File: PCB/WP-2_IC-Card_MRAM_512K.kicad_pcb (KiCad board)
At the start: 2 copper layers, 54 x 54 mm, 38 parts, among them J1 SMS-138-01-G-S, SW1 CUS-14TB, U1 MR2A08xxYSxxx, U2 MIC5317-3.3YD5, U3 4245, U4 4245, U5 4245, U6 4245

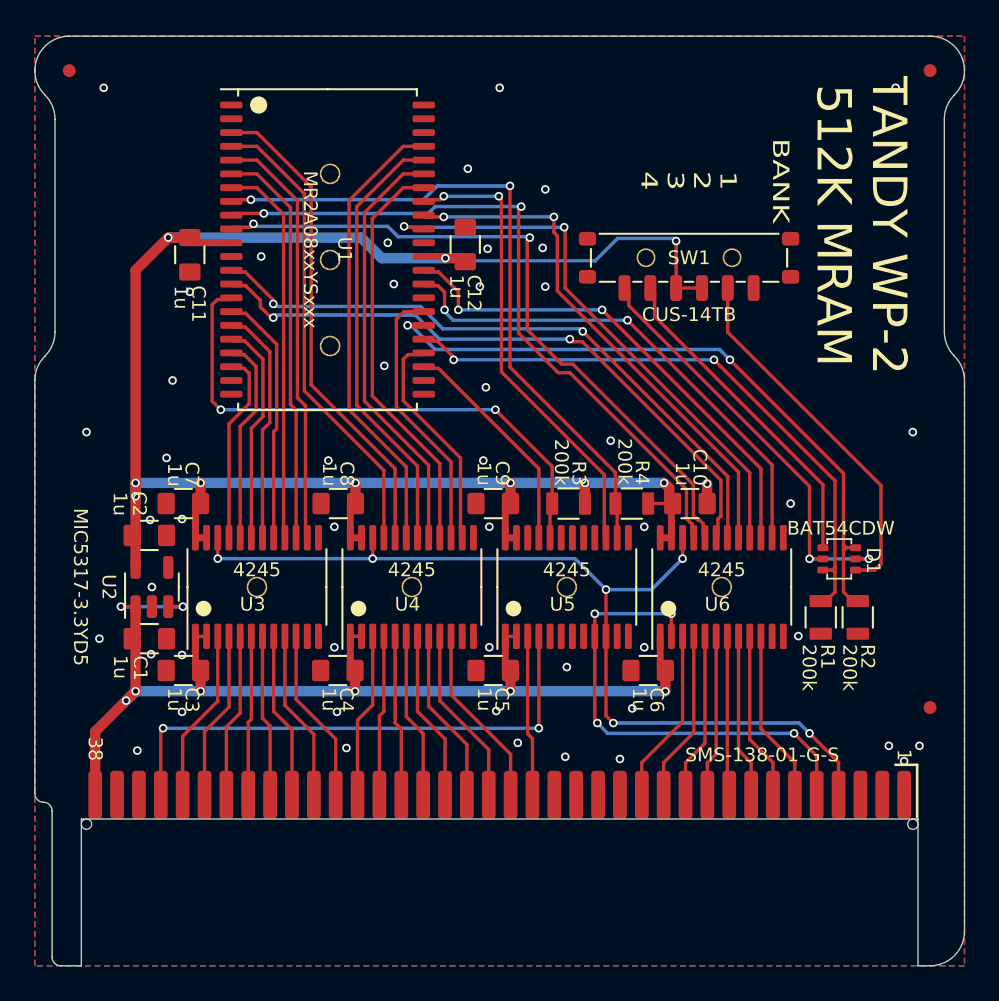
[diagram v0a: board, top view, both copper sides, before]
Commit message: local symbol & footprint library organization, add shielded mram version
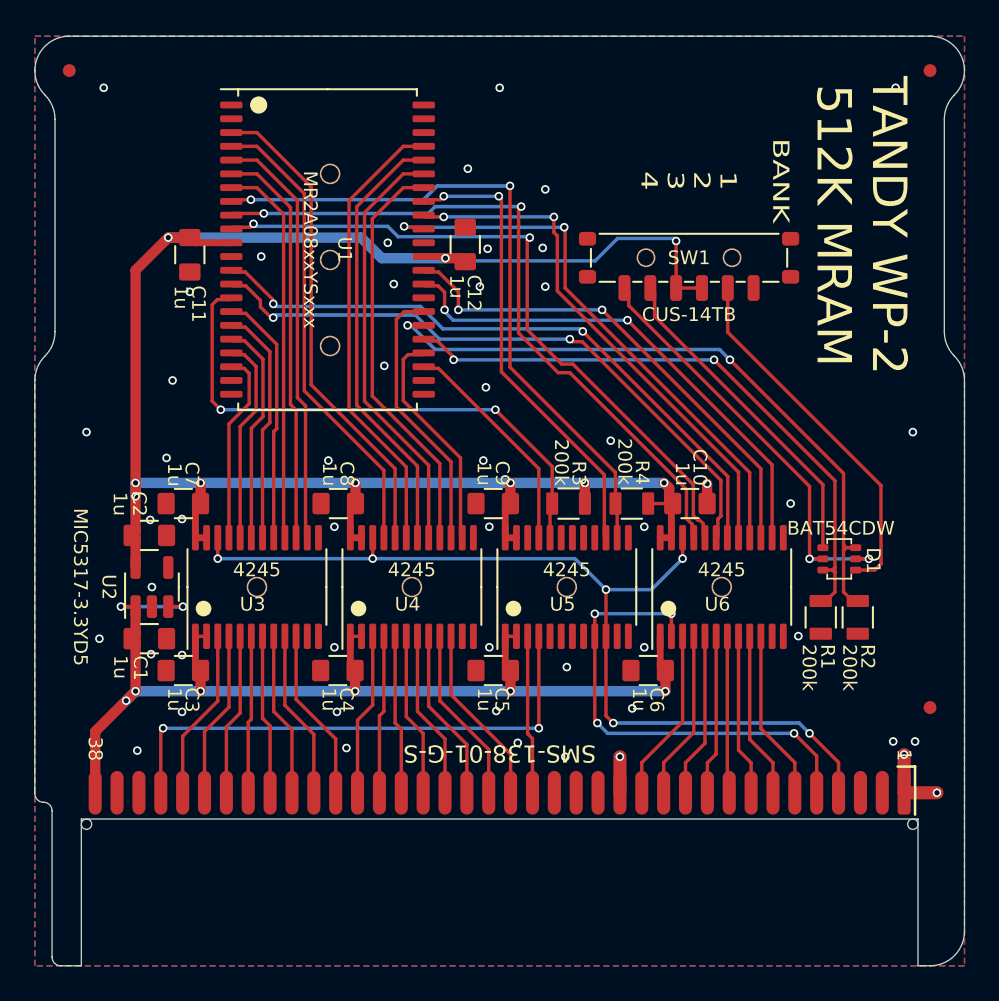
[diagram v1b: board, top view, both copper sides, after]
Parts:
- removed the REF** at (159.9, 114.0)
- removed the REF** at (135.9, 95.2)
- removed the REF** at (112.0, 114.0)
- added N1: WP-2_IC-Card_Cover_MRAM_512, 000_LOCAL:WP-2_IC_Card_Cover_MRAM_512, F.Cu at (135.9, 95.2)
- added REF**: npth_0.6mm, 000_LOCAL:npth_0.6mm, F.Cu at (159.9, 114.0)
- added REF**: npth_0.6mm, 000_LOCAL:npth_0.6mm, F.Cu at (112.0, 114.0)
- C1, C10, C11, C12, C2, C3, C4, C5, C6, C7, C8, C9: footprint 0_LOCAL:C_0805_1mm -> 000_LOCAL:C_0805_1mm
- D1: footprint 0_LOCAL:TSSOP-6-symmetric -> 000_LOCAL:TSSOP-6-symmetric
- J1: footprint 0_LOCAL:SMS-138-01-x-x_edge -> 000_LOCAL:SMS-138-01-x-x_pcb_edge
- R1, R2, R3, R4: footprint 0_LOCAL:R_0805 -> 000_LOCAL:R_0805
- REF** (x7): footprint 0_LOCAL:pth_wash_1mm -> 000_LOCAL:pth_wash_1mm
- REF** (x3): footprint 0_LOCAL:Fiducial_0.75mm_Mask1.5mm -> 000_LOCAL:Fiducial_0.75mm_Mask1.5mm
- SW1: footprint 0_LOCAL:SW_SP4T_CUS-14B pth -> 000_LOCAL:SW_SP4T_CUS-14B pth
- U1: footprint 0_LOCAL:TSOP-II-44_10.16x18.41mm_P0.8mm -> 000_LOCAL:TSOP-II-44_10.16x18.41mm_P0.8mm
- U2: footprint 0_LOCAL:TSOT-23-5 -> 000_LOCAL:TSOT-23-5
- U3, U4, U5, U6: footprint 0_LOCAL:TSSOP-24_4.4x7.8mm_P0.65mm -> 000_LOCAL:TSSOP-24_4.4x7.8mm_P0.65mm
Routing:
- net GND: track 1.15 -> 7.37 mm, vias 50 -> 51
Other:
- board text added: "BOARD OUTLINE"

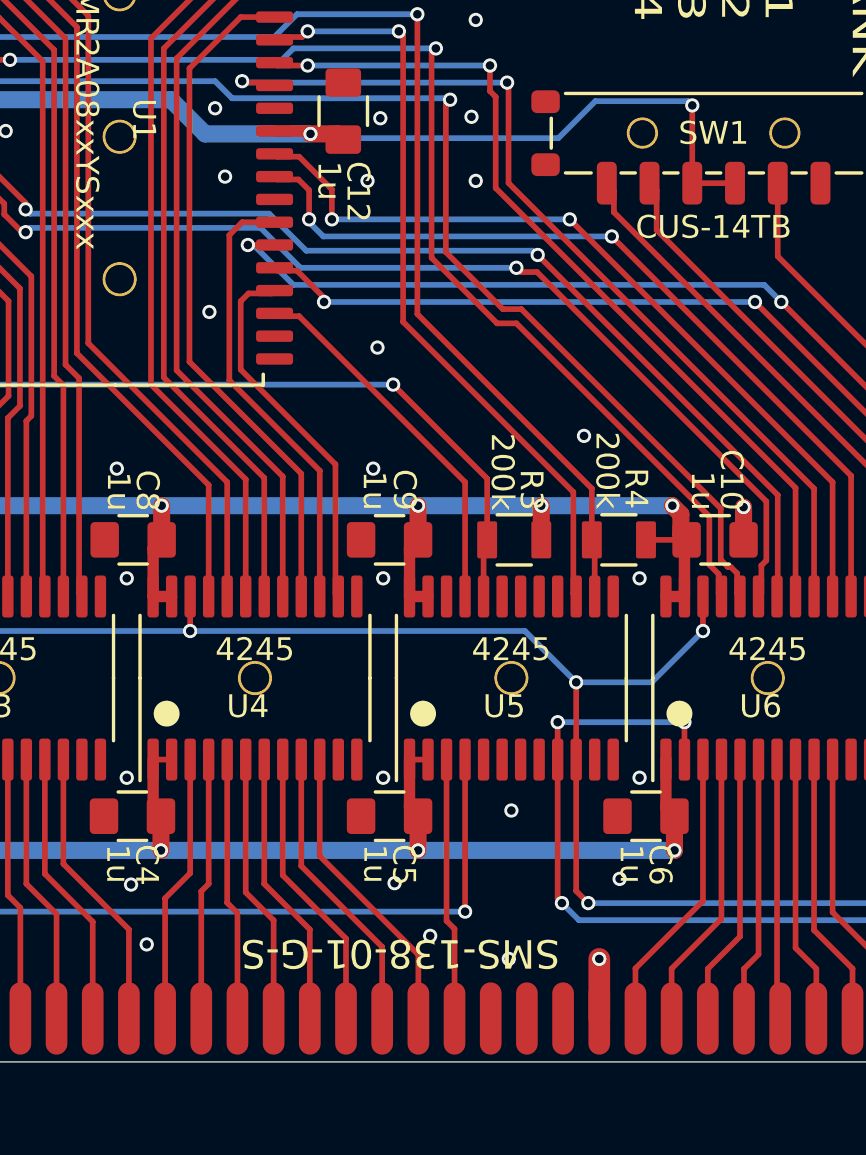
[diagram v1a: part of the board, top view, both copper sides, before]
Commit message: cleanup names, cover inside corner reliefs
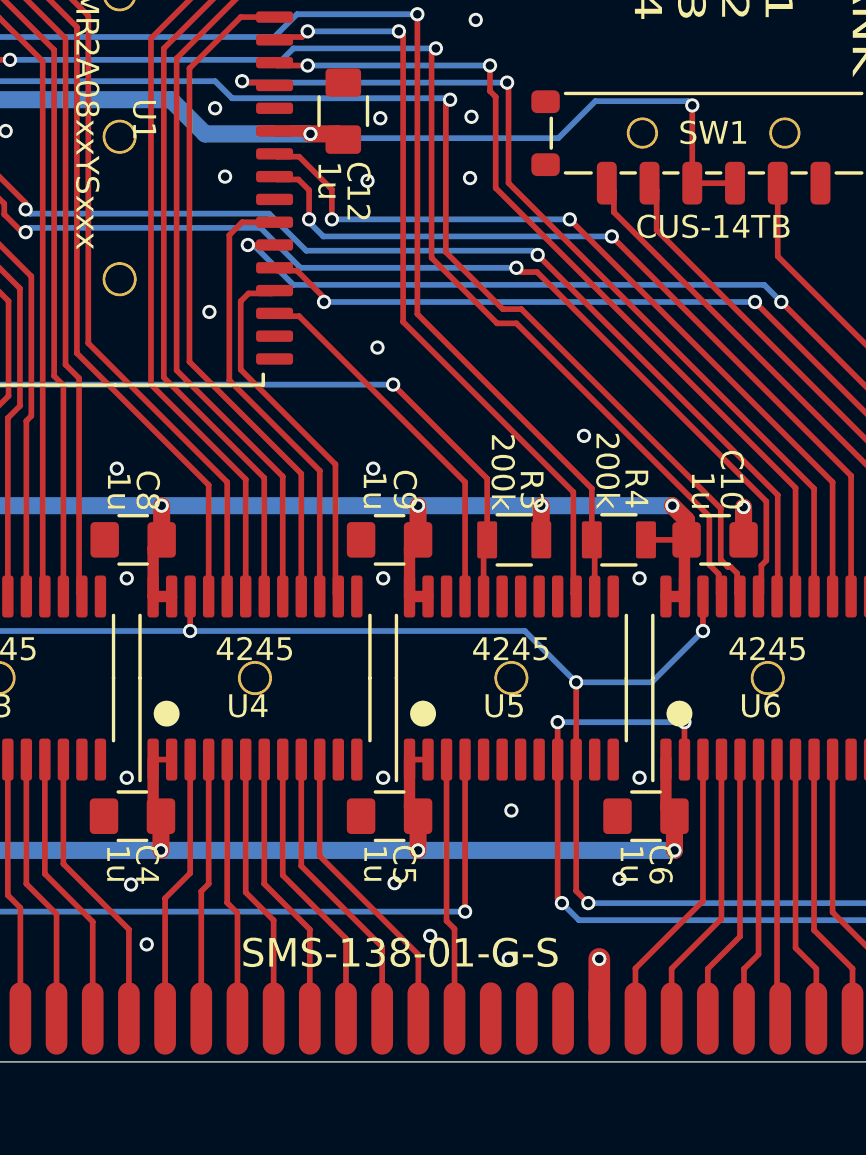
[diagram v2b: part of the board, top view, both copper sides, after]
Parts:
- N1: footprint 000_LOCAL:WP-2_IC_Card_Cover_MRAM_512 -> 000_LOCAL:WP-2_IC-Card_Cover_MRAM_512

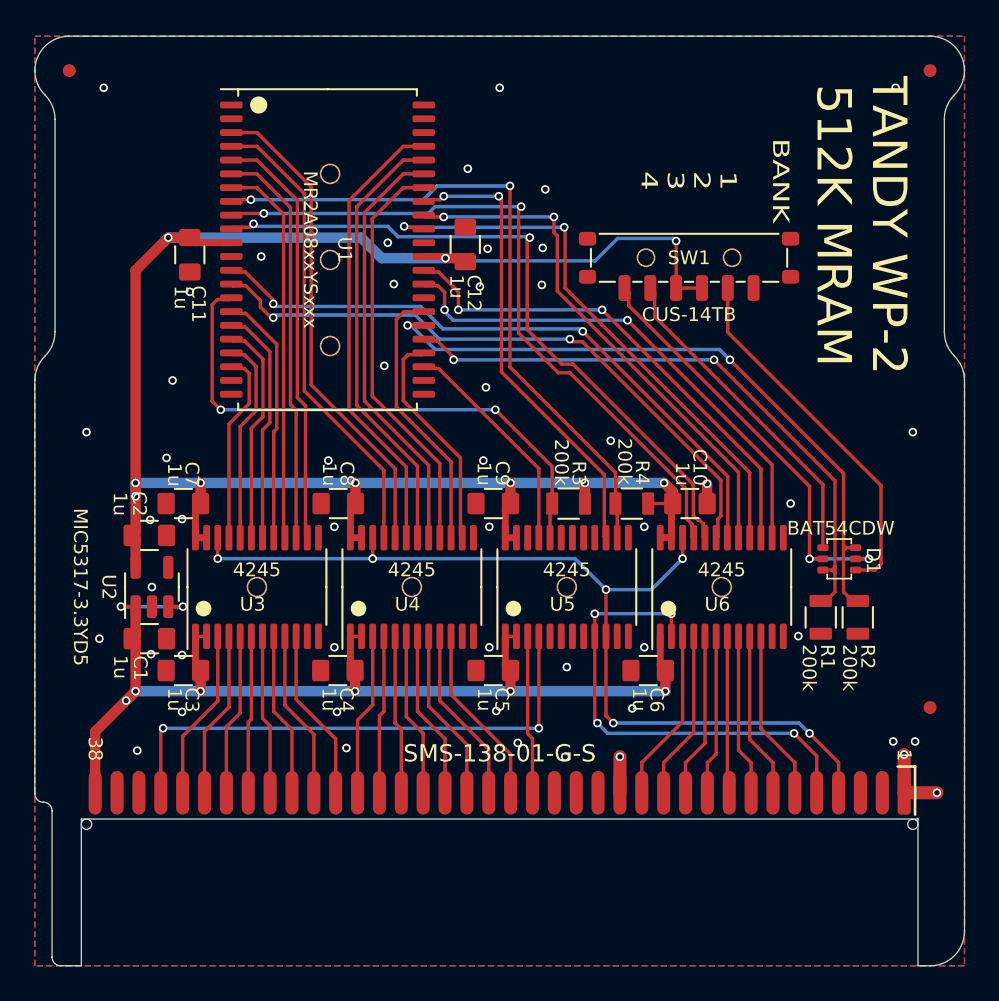
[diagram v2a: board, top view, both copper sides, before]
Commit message: redraw board outline and copy to all boards
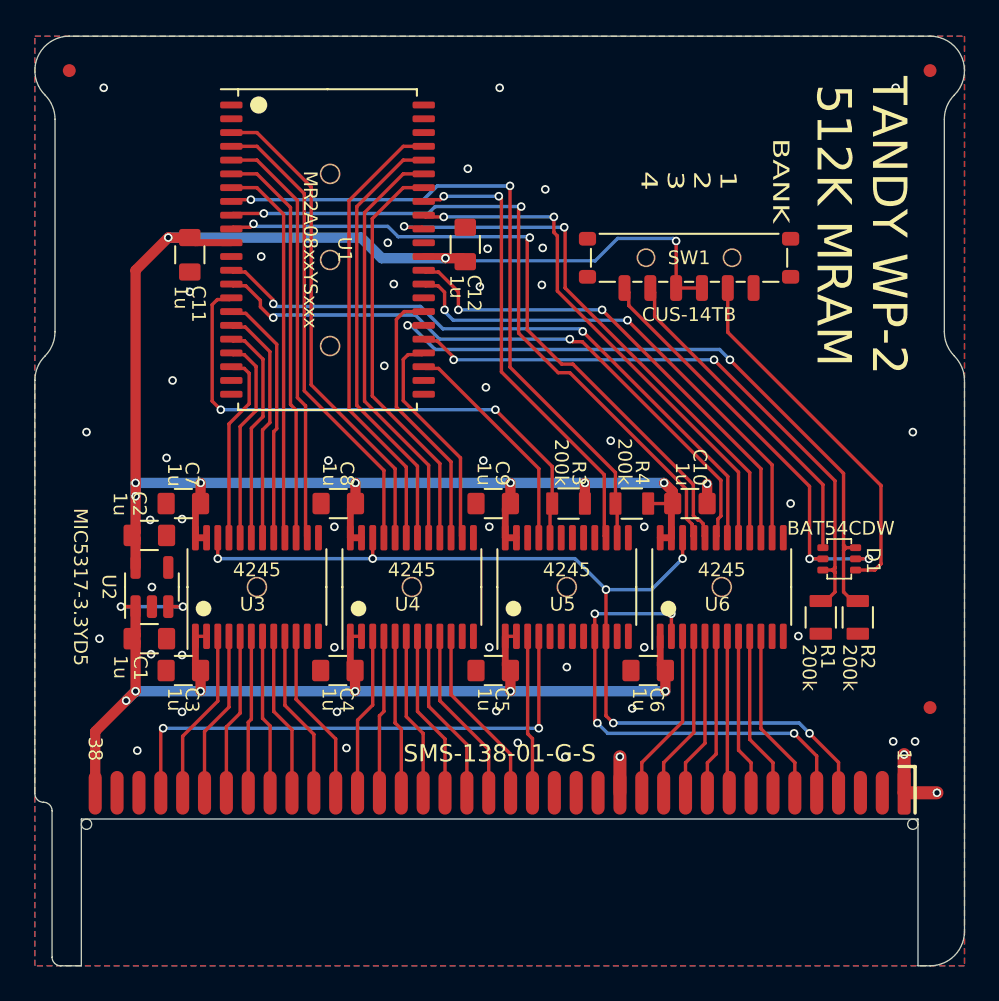
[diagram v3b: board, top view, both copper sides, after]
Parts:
- removed the REF** at (160.9, 70.2)
- removed the REF** at (111.0, 70.2)
- removed the REF** at (160.9, 107.2)
- added REF**: Fiducial_1.5, 000_LOCAL:Fiducial_1.5, F.Cu at (111.0, 70.2)
- added REF**: Fiducial_1.5, 000_LOCAL:Fiducial_1.5, F.Cu at (160.9, 70.2)
- added REF**: Fiducial_1.5, 000_LOCAL:Fiducial_1.5, F.Cu at (160.9, 107.2)
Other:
- outline, holes or cut-outs redrawn

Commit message: rom wren sw, boms, footprints, shielded mram
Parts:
- C1, C10, C11, C12, C2, C3, C4, C5, C6, C7, C8, C9: footprint 000_LOCAL:C_0805_1mm -> 000_LOCAL:C_0805
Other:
- board text added: "Max PCB Thickness: 1.2mm"

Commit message: update covers for flash & mram with bank sw & write sw
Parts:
- N1: value WP-2_IC-Card_Cover_MRAM_512 -> WP-2_IC-Card_Cover_MRAM; footprint 000_LOCAL:WP-2_IC-Card_Cover_MRAM_512 -> 000_LOCAL:WP-2_IC-Card_Cover_MRAM
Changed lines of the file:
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@@
 		)
 	)
-	(footprint "000_LOCAL:WP-2_IC-Card_Cover_MRAM_512"
+	(footprint "000_LOCAL:WP-2_IC-Card_Cover_MRAM"
 		(layer "F.Cu")
 		(at 135.95 95.245)
@@
 			)
 		)
-		(property "Value" "WP-2_IC-Card_Cover_MRAM_512"
+		(property "Value" "WP-2_IC-Card_Cover_MRAM"
 			(at 0 2.5 0)
 			(unlocked yes)
@@
 			)
 		)
-		(property "Footprint" "000_LOCAL:WP-2_IC-Card_Cover_MRAM_512"
+		(property "Footprint" "000_LOCAL:WP-2_IC-Card_Cover_MRAM"
 			(at 0 0 0)
 			(layer "F.Fab")
@@
 		)
 		(group ""
-			(members "064e2289-8725-424f-af75-2875d593f422" "0ecc3ac9-0f7c-4882-b979-c0b65c369c15"
-				"15cc2823-d863-444e-b872-a24124e97947" "2e10ffd8-0078-49b0-89f2-674e35fd72cf"
-				"2e1f69b4-c544-4462-84ea-88bb9873b4dc" "3a4f7540-e968-4cc1-b8dd-aa24f2b631bf"
-				"3e3a6dc9-5e3b-48e0-9b3a-976cf6c4b756" "3e828dc9-2256-40d0-b903-a52bf5159ad2"
-				"45225cc2-07a4-4030-9b55-4cf9477fca11" "478e9877-5d56-4bc1-83c7-3360ed17498c"
-				"5ec86082-3a74-46d7-a341-53b2aba4d5bf" "60fcdfd0-c96d-426f-ba19-94dd09a30013"
-				"66beac26-f96c-467c-bf64-c12a2eba84f9" "679f3a14-75be-411d-9d70-139d8df23bc9"
-				"8a49aad4-1dd4-428c-9bda-cb10e65cedc7" "9c2a2d8a-2815-4420-b1af-9adde339e31f"
-				"a4f3da45-917f-4a82-be93-9acdae7c5fe8" "c1e61f30-8cc9-4f1d-a917-ed23a45c027a"
-				"c2cd2768-3fbc-4f1e-b6fa-e84a1619cb04" "cd9e599f-d2f9-4c15-aa85-6e2c3c8c1cf1"
-				"d2502a3e-4688-4ed6-bef6-b168ec394d3d" "d527bd4f-3d14-48dd-8c45-cf6978fde304"
-				"e3269d09-26df-46f8-b516-1453c2d6a4f3" "eb8bc6bb-caf2-4180-a2c6-a3827c3df891"
-				"fbcf17dd-96f1-4540-81ad-928ba49bb0c3" "ff5f55f9-aa38-4fb0-9a89-7b70222f2c32"
-			)
-		)
-		(model "${KIPRJMOD}/000_LOCAL.pretty/3d/WP-2_IC-Card_Cover_MRAM_512_slider.step"
+			(members "0d06d361-0cdf-4fda-bed7-766a85362cb0" "112860ed-a133-4b83-a426-6e77649f389e"
+				"16ff6909-c628-4db1-9cc9-ea908b9e4782" "2778f4d6-5af6-49e9-a00a-5eedfdac6719"
+				"289cefc8-f801-4c60-88f2-f655e68da7ee" "2ef8791b-1efd-4a55-b8f8-948a79300c30"
+				"3075feb8-6e69-43c4-ad02-8fda81bf36c6" "411a2ea6-0b8f-44a5-a5a5-8bb0800539b6"
+				"42026ae4-0654-4997-b024-036946fc18ea" "469894c5-4274-4fc8-8c57-fa5008982230"
+				"4d089442-653a-4aee-9d91-e881da9dcd41" "59108e57-4817-41d9-8b88-83b953294e75"
+				"64ddc95e-814b-4172-8dca-3285f2fb80de" "66646d16-4281-410e-9d2c-65dd7e6c8e56"
+				"6bac38c8-a248-44c2-8dac-5ba9ac8dd730" "8de7bb19-a20b-415b-b3c6-bfc7d523fab9"
+				"9032b632-2ed6-4408-b3a5-c4f01fa5d057" "a2295315-2f93-406d-ab4b-52217990f18d"
+				"b45cc4e4-2fe4-4097-8af9-259b5c4d23d8" "bfdedd39-873a-49b4-b11c-ee420aa64c2a"
+				"c8b9207b-3cab-4a61-aef0-b3a1f0df678c" "f0f60a2e-9bba-4604-8e86-a0357d0c2d33"
+				"f34eec05-323d-40bd-a34d-f5b65845741b" "f5d76fea-3ebc-4d62-a5d3-6ff6acd9c09f"
+				"f710e011-2823-446d-a4f9-6097556dbd82" "fa73f1c6-196d-43ab-86e4-a527304648ba"
+			)
+		)
+		(model "${KIPRJMOD}/000_LOCAL.pretty/3d/WP_2_IC_Card_Cover_MRAM_bank_finger.step"
+			(hide yes)
 			(offset
 				(xyz 0 0 0)
@@
 			)
 		)
-		(model "${KIPRJMOD}/000_LOCAL.pretty/3d/WP-2_IC-Card_Cover_MRAM_512_window.step"
-			(hide yes)
+		(model "${KIPRJMOD}/000_LOCAL.pretty/3d/WP_2_IC_Card_Cover_MRAM_bank_slider.step"
 			(offset
+				(xyz 0 0 0)
+			)
+			(scale
+				(xyz 1 1 1)
+			)
+			(rotate
+				(xyz 0 0 0)
+			)
+		)
+		(model "${KIPRJMOD}/000_LOCAL.pretty/3d/WP_2_IC_Card_Cover_MRAM_no_bank.step"
+			(hide yes)
+			(offset
